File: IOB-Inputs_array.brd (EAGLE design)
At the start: 104.1 x 106.7 mm, 81 parts

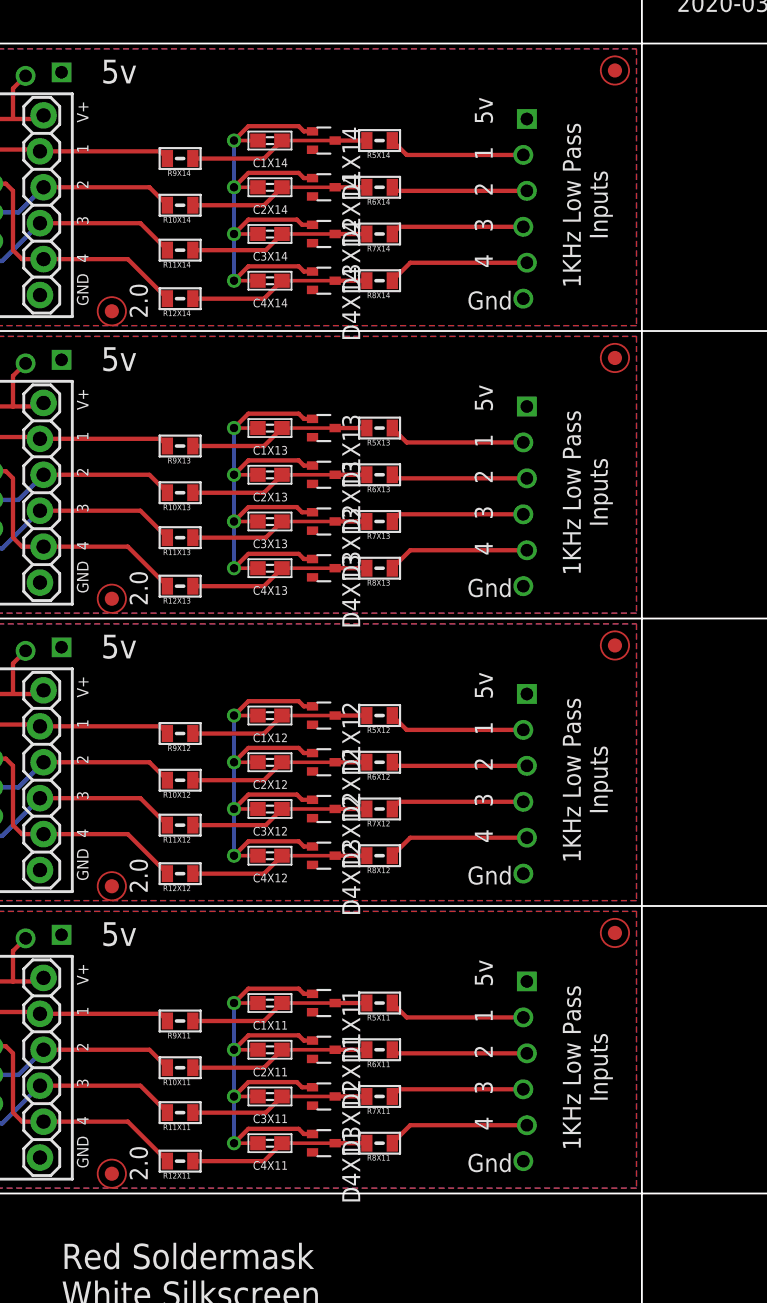
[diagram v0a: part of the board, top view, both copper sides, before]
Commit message: fixed SPCoast.lbr diode orientation
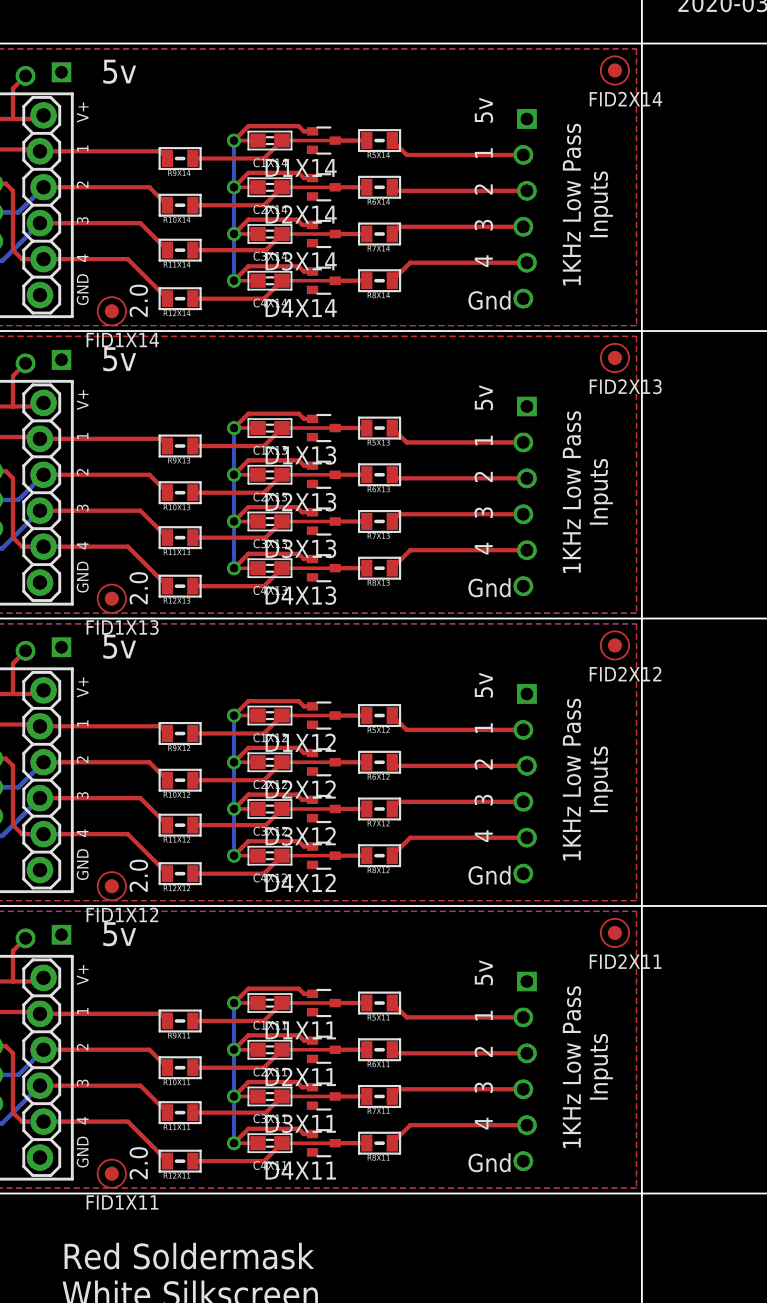
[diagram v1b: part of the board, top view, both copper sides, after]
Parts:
- turned D1X11 to 180 degrees
- turned D1X12 to 180 degrees
- turned D1X13 to 180 degrees
- turned D1X14 to 180 degrees
- turned D2X11 to 180 degrees
- turned D2X12 to 180 degrees
- turned D2X13 to 180 degrees
- turned D2X14 to 180 degrees
- turned D3X11 to 180 degrees
- turned D3X12 to 180 degrees
- turned D3X13 to 180 degrees
- turned D3X14 to 180 degrees
- turned D4X11 to 180 degrees
- turned D4X12 to 180 degrees
- turned D4X13 to 180 degrees
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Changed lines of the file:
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@@
 <element name="C3X11" library="SPCoast" package="0603-CAP" value="" x="52.451" y="15.748" rot="R180"/>
 <element name="C4X11" library="SPCoast" package="0603-CAP" value="" x="52.451" y="12.446" rot="R180"/>
-<element name="D1X11" library="SPCoast" package="SOT323R" value="" x="56.261" y="22.352" rot="R270"/>
-<element name="D2X11" library="SPCoast" package="SOT323R" value="" x="56.261" y="19.05" rot="R270"/>
-<element name="D3X11" library="SPCoast" package="SOT323R" value="" x="56.261" y="15.748" rot="R270"/>
-<element name="D4X11" library="SPCoast" package="SOT323R" value="" x="56.261" y="12.446" rot="R270"/>
+<element name="D1X11" library="SPCoast" package="SOT323R" value="" x="56.261" y="22.352" rot="R180"/>
+<element name="D2X11" library="SPCoast" package="SOT323R" value="" x="56.261" y="19.05" rot="R180"/>
+<element name="D3X11" library="SPCoast" package="SOT323R" value="" x="56.261" y="15.748" rot="R180"/>
+<element name="D4X11" library="SPCoast" package="SOT323R" value="" x="56.261" y="12.446" rot="R180"/>
 <element name="FID1X11" library="SPCoast" package="FIDUCIAL_1MM" value="" x="41.275" y="10.287"/>
 <element name="FID2X11" library="SPCoast" package="FIDUCIAL_1MM" value="" x="76.835" y="27.305"/>
@@
 <element name="C3X12" library="SPCoast" package="0603-CAP" value="" x="52.451" y="36.068" rot="R180"/>
 <element name="C4X12" library="SPCoast" package="0603-CAP" value="" x="52.451" y="32.766" rot="R180"/>
-<element name="D1X12" library="SPCoast" package="SOT323R" value="" x="56.261" y="42.672" rot="R270"/>
-<element name="D2X12" library="SPCoast" package="SOT323R" value="" x="56.261" y="39.37" rot="R270"/>
-<element name="D3X12" library="SPCoast" package="SOT323R" value="" x="56.261" y="36.068" rot="R270"/>
-<element name="D4X12" library="SPCoast" package="SOT323R" value="" x="56.261" y="32.766" rot="R270"/>
+<element name="D1X12" library="SPCoast" package="SOT323R" value="" x="56.261" y="42.672" rot="R180"/>
+<element name="D2X12" library="SPCoast" package="SOT323R" value="" x="56.261" y="39.37" rot="R180"/>
+<element name="D3X12" library="SPCoast" package="SOT323R" value="" x="56.261" y="36.068" rot="R180"/>
+<element name="D4X12" library="SPCoast" package="SOT323R" value="" x="56.261" y="32.766" rot="R180"/>
 <element name="FID1X12" library="SPCoast" package="FIDUCIAL_1MM" value="" x="41.275" y="30.607"/>
 <element name="FID2X12" library="SPCoast" package="FIDUCIAL_1MM" value="" x="76.835" y="47.625"/>
@@
 <element name="C3X13" library="SPCoast" package="0603-CAP" value="" x="52.451" y="56.388" rot="R180"/>
 <element name="C4X13" library="SPCoast" package="0603-CAP" value="" x="52.451" y="53.086" rot="R180"/>
-<element name="D1X13" library="SPCoast" package="SOT323R" value="" x="56.261" y="62.992" rot="R270"/>
-<element name="D2X13" library="SPCoast" package="SOT323R" value="" x="56.261" y="59.69" rot="R270"/>
-<element name="D3X13" library="SPCoast" package="SOT323R" value="" x="56.261" y="56.388" rot="R270"/>
-<element name="D4X13" library="SPCoast" package="SOT323R" value="" x="56.261" y="53.086" rot="R270"/>
+<element name="D1X13" library="SPCoast" package="SOT323R" value="" x="56.261" y="62.992" rot="R180"/>
+<element name="D2X13" library="SPCoast" package="SOT323R" value="" x="56.261" y="59.69" rot="R180"/>
+<element name="D3X13" library="SPCoast" package="SOT323R" value="" x="56.261" y="56.388" rot="R180"/>
+<element name="D4X13" library="SPCoast" package="SOT323R" value="" x="56.261" y="53.086" rot="R180"/>
 <element name="FID1X13" library="SPCoast" package="FIDUCIAL_1MM" value="" x="41.275" y="50.927"/>
 <element name="FID2X13" library="SPCoast" package="FIDUCIAL_1MM" value="" x="76.835" y="67.945"/>
@@
 <element name="C3X14" library="SPCoast" package="0603-CAP" value="" x="52.451" y="76.708" rot="R180"/>
 <element name="C4X14" library="SPCoast" package="0603-CAP" value="" x="52.451" y="73.406" rot="R180"/>
-<element name="D1X14" library="SPCoast" package="SOT323R" value="" x="56.261" y="83.312" rot="R270"/>
-<element name="D2X14" library="SPCoast" package="SOT323R" value="" x="56.261" y="80.01" rot="R270"/>
-<element name="D3X14" library="SPCoast" package="SOT323R" value="" x="56.261" y="76.708" rot="R270"/>
-<element name="D4X14" library="SPCoast" package="SOT323R" value="" x="56.261" y="73.406" rot="R270"/>
+<element name="D1X14" library="SPCoast" package="SOT323R" value="" x="56.261" y="83.312" rot="R180"/>
+<element name="D2X14" library="SPCoast" package="SOT323R" value="" x="56.261" y="80.01" rot="R180"/>
+<element name="D3X14" library="SPCoast" package="SOT323R" value="" x="56.261" y="76.708" rot="R180"/>
+<element name="D4X14" library="SPCoast" package="SOT323R" value="" x="56.261" y="73.406" rot="R180"/>
 <element name="FID1X14" library="SPCoast" package="FIDUCIAL_1MM" value="" x="41.275" y="71.247"/>
 <element name="FID2X14" library="SPCoast" package="FIDUCIAL_1MM" value="" x="76.835" y="88.265"/>

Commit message: Added missing values
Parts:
- C1X11, C1X12, C1X13, C1X14, C2X11, C2X12, C2X13, C2X14, C3X11, C3X12, C3X13, C3X14, C4X11, C4X12, C4X13, C4X14: value (none) -> 0.1uF
- R10X11, R10X12, R10X13, R10X14, R11X11, R11X12, R11X13, R11X14, R12X11, R12X12, R12X13, R12X14, R9X11, R9X12, R9X13, R9X14: value (none) -> 82R
- R5X11, R5X12, R5X13, R5X14, R6X11, R6X12, R6X13, R6X14, R7X11, R7X12, R7X13, R7X14, R8X11, R8X12, R8X13, R8X14: value (none) -> 1k0

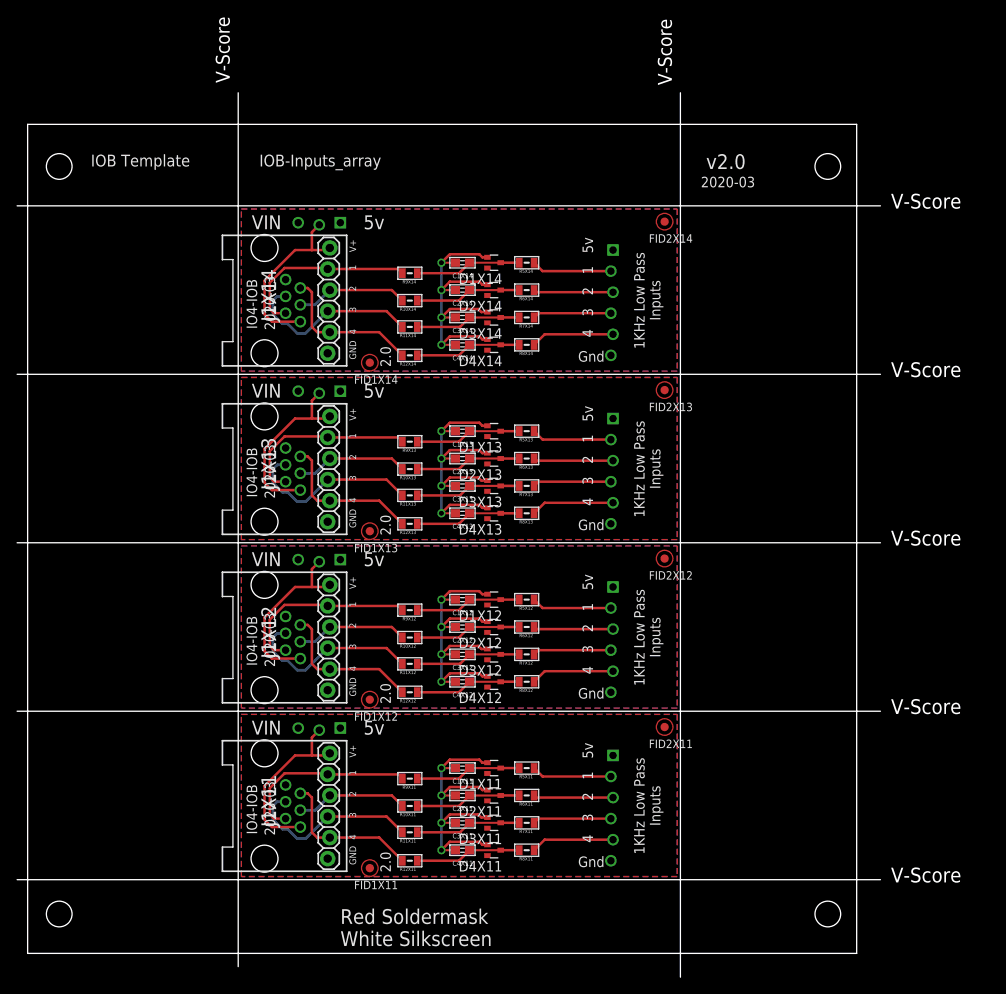
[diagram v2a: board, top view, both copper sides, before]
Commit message: Replaced too small BAT54S SOT23R footprint with SOT23
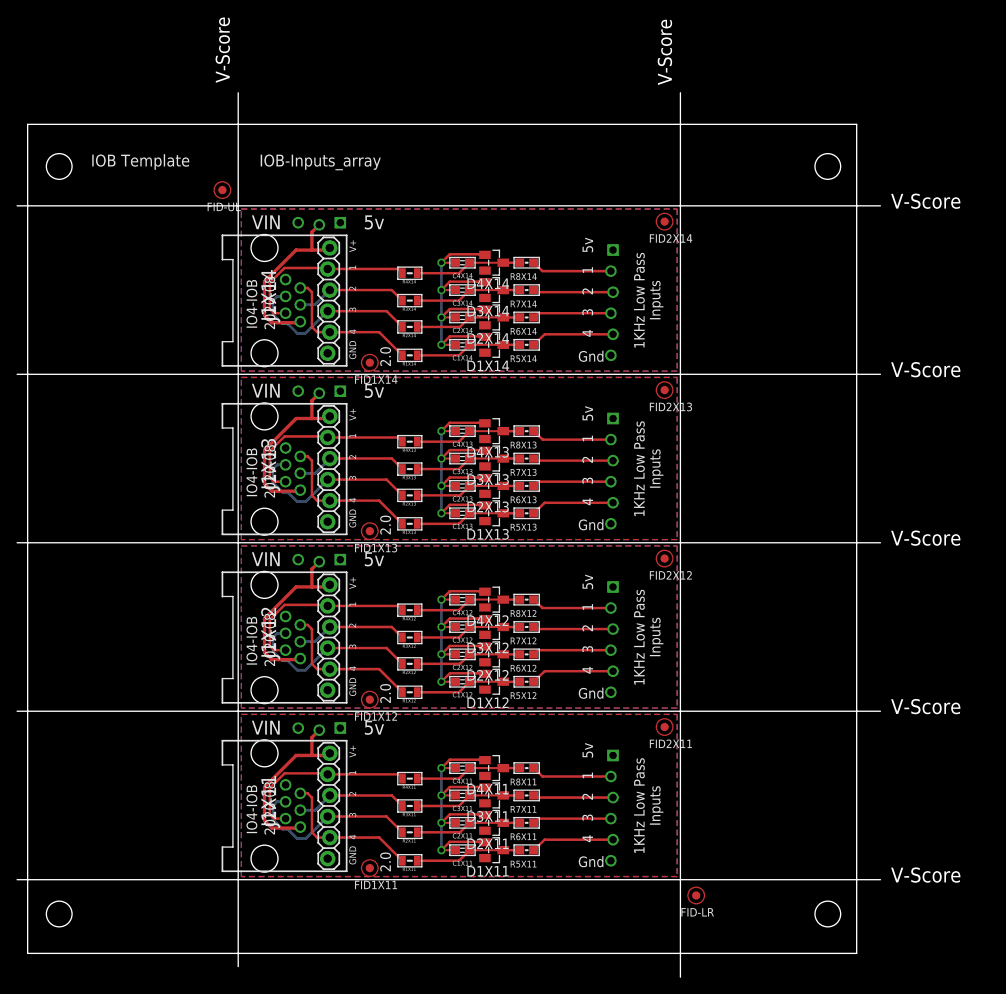
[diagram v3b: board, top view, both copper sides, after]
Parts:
- added FID-LR, FID-UL: FIDUCIAL, SPCoast:FIDUCIAL_1MM
- C1X11, C1X12, C1X13, C1X14, C2X11, C2X12, C2X13, C2X14, C3X11, C3X12, C3X13, C3X14, C4X11, C4X12, C4X13, C4X14: value 0.1uF -> 0.01uF
- D1X11, D1X12, D1X13, D1X14, D2X11, D2X12, D2X13, D2X14, D3X11, D3X12, D3X13, D3X14, D4X11, D4X12, D4X13, D4X14: value (none) -> BAT54S; device SPCoast:SOT323R -> SPCoast:SOT23
- FID1X11, FID1X12, FID1X13, FID1X14, FID2X11, FID2X12, FID2X13, FID2X14: value (none) -> FIDUCIAL
- IOBX11, IOBX12, IOBX13, IOBX14: value (none) -> CONNECTOR-IO4-IOBFULL
- J1X11, J1X12, J1X13, J1X14: value (none) -> RJ12/6
- R5X11, R5X12, R5X13, R5X14, R6X11, R6X12, R6X13, R6X14, R7X11, R7X12, R7X13, R7X14, R8X11, R8X12, R8X13, R8X14: value 1k0 -> 1K0; device SPCoast:0805-RES -> SPCoast:0603-RES
- moved C1X11 9.91 mm to (52.5, 12.4)
- moved C4X11 9.91 mm to (52.5, 22.4)
- moved D1X11 9.91 mm to (56.3, 12.4)
- moved D4X11 9.91 mm to (56.3, 22.4)
- moved R5X11 9.91 mm to (60.2, 12.4)
- moved R8X11 9.91 mm to (60.2, 22.4)
- moved C1X12 9.91 mm to (52.5, 32.8)
- moved C1X13 9.91 mm to (52.5, 53.1)
- moved C4X12 9.91 mm to (52.5, 42.7)
- moved C4X13 9.91 mm to (52.5, 63.0)
- moved D1X12 9.91 mm to (56.3, 32.8)
- moved D1X13 9.91 mm to (56.3, 53.1)
- moved D4X12 9.91 mm to (56.3, 42.7)
- moved D4X13 9.91 mm to (56.3, 63.0)
- moved R5X12 9.91 mm to (60.2, 32.8)
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- renumbered R10X11 to R3X11, R10X12 to R3X12, R10X13 to R3X13, R10X14 to R3X14, R11X11 to R2X11, R11X12 to R2X12, R11X13 to R2X13, R11X14 to R2X14, R12X1 to R8X1, R12X11 to R1X11, R12X12 to R1X12, R12X13 to R1X13, R12X14 to R1X14, R9X11 to R4X11, R9X12 to R4X12, R9X13 to R4X13, R9X14 to R4X14
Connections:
- net N$10X11: now also C1X11.1, D1X11.3, R5X11.2; no longer C4X11.1, D4X11.2, R8X11.2
- net N$10X12: now also C1X12.1, D1X12.3, R5X12.2; no longer C4X12.1, D4X12.2, R8X12.2
- net N$10X13: now also C1X13.1, D1X13.3, R5X13.2; no longer C4X13.1, D4X13.2, R8X13.2
- net N$10X14: now also C1X14.1, D1X14.3, R5X14.2; no longer C4X14.1, D4X14.2, R8X14.2
- net N$12X11: now also C2X11.1, D2X11.3, R6X11.2; no longer C3X11.1, D3X11.2, R7X11.2
- net N$12X12: now also C2X12.1, D2X12.3, R6X12.2; no longer C3X12.1, D3X12.2, R7X12.2
- net N$12X13: now also C2X13.1, D2X13.3, R6X13.2; no longer C3X13.1, D3X13.2, R7X13.2
- net N$12X14: now also C2X14.1, D2X14.3, R6X14.2; no longer C3X14.1, D3X14.2, R7X14.2
- net N$13X11: now also C3X11.1, D3X11.3, R7X11.2; no longer C2X11.1, D2X11.2, R6X11.2
- net N$13X12: now also C3X12.1, D3X12.3, R7X12.2; no longer C2X12.1, D2X12.2, R6X12.2
- net N$13X13: now also C3X13.1, D3X13.3, R7X13.2; no longer C2X13.1, D2X13.2, R6X13.2
- net N$13X14: now also C3X14.1, D3X14.3, R7X14.2; no longer C2X14.1, D2X14.2, R6X14.2
- net N$14X11: now also C4X11.1, D4X11.3, R8X11.2; no longer C1X11.1, D1X11.2, R5X11.2
- net N$14X12: now also C4X12.1, D4X12.3, R8X12.2; no longer C1X12.1, D1X12.2, R5X12.2
- net N$14X13: now also C4X13.1, D4X13.3, R8X13.2; no longer C1X13.1, D1X13.2, R5X13.2
- net N$14X14: now also C4X14.1, D4X14.3, R8X14.2; no longer C1X14.1, D1X14.2, R5X14.2
- net P1X11: now also R8X11.1; no longer R5X11.1
- net P1X12: now also R8X12.1; no longer R5X12.1
- net P1X13: now also R8X13.1; no longer R5X13.1
- net P1X14: now also R8X14.1; no longer R5X14.1
- net P2X11: now also R7X11.1; no longer R6X11.1
- net P2X12: now also R7X12.1; no longer R6X12.1
- net P2X13: now also R7X13.1; no longer R6X13.1
- net P2X14: now also R7X14.1; no longer R6X14.1
- net P3X11: now also R6X11.1; no longer R7X11.1
- net P3X12: now also R6X12.1; no longer R7X12.1
- net P3X13: now also R6X13.1; no longer R7X13.1
- net P3X14: now also R6X14.1; no longer R7X14.1
- net P4X11: now also R5X11.1; no longer R8X11.1
- net P4X12: now also R5X12.1; no longer R8X12.1
- net P4X13: now also R5X13.1; no longer R8X13.1
- net P4X14: now also R5X14.1; no longer R8X14.1
- net VCCX11: now also D1X11.2, D2X11.2, D3X11.2, D4X11.2; no longer D1X11.3, D2X11.3, D3X11.3, D4X11.3
- net VCCX12: now also D1X12.2, D2X12.2, D3X12.2, D4X12.2; no longer D1X12.3, D2X12.3, D3X12.3, D4X12.3
- net VCCX13: now also D1X13.2, D2X13.2, D3X13.2, D4X13.2; no longer D1X13.3, D2X13.3, D3X13.3, D4X13.3
- net VCCX14: now also D1X14.2, D2X14.2, D3X14.2, D4X14.2; no longer D1X14.3, D2X14.3, D3X14.3, D4X14.3
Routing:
- net GNDX14: track 41.2 -> 40.4 mm
- net GNDX13: track 41.2 -> 40.4 mm
- net GNDX12: track 41.2 -> 40.4 mm
- net GNDX11: track 41.2 -> 40.4 mm
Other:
- board text added: "2020-08"
- board text added: "Red Headers"
- board text removed: "2020-03"
- board text removed: "v2.0"
